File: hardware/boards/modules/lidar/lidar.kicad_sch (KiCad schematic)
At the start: 26 parts, among them J1 Conn_01x04_Socket, J2 Lidar, J3 Conn_01x03_Socket, J4 Conn_01x03_Socket, J5 Conn_01x03_Socket, J6 Conn_01x03_Socket, J7 Conn_01x05_Socket, Q1 AO3401A, SW1 SW_Push, U1 ATmega128A-A, Y1 8MHz

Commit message: REFACTO relinked every kicad projects
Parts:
- Q1: footprint Package_TO_SOT_SMD:SOT-23_Handsoldering -> Package_TO_SOT_SMD:SOT-23
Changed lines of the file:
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@@
+	)
+	(junction
+		(at 39.37 97.79)
+		(diameter 0)
+		(color 0 0 0 0)
 	)
 	(junction
@@
 	(wire
 		(pts
+			(xy 39.37 67.31) (xy 39.37 97.79)
+		)
+		(stroke
+			(width 0)
+			(type default)
+		)
+	)
+	(wire
+		(pts
 			(xy 162.56 152.4) (xy 162.56 140.97)
 		)
@@
 	(wire
 		(pts
+			(xy 30.48 67.31) (xy 39.37 67.31)
+		)
+		(stroke
+			(width 0)
+			(type default)
+		)
+	)
+	(wire
+		(pts
 			(xy 241.3 147.32) (xy 243.84 147.32)
 		)
@@
 	(wire
 		(pts
-			(xy 29.21 97.79) (xy 24.13 97.79)
+			(xy 24.13 97.79) (xy 30.48 97.79)
+		)
+		(stroke
+			(width 0)
+			(type default)
+		)
+	)
+	(wire
+		(pts
+			(xy 30.48 97.79) (xy 30.48 67.31)
 		)
 		(stroke
@@
 			)
 		)
-		(property "Footprint" "Package_TO_SOT_SMD:SOT-23_Handsoldering"
+		(property "Footprint" "Package_TO_SOT_SMD:SOT-23"
 			(at 238.76 81.915 0)
 			(effects

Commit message: updated main points of the lidar module schematic
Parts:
- removed J2: Lidar, Connector_PinHeader_2.54mm:PinHeader_1x04_P2.54mm_Vertical, symbol Connector:Conn_01x04_Socket
- removed J6: Conn_01x03_Socket, Connector_PinHeader_2.54mm:PinHeader_1x03_P2.54mm_Vertical, symbol Connector:Conn_01x03_Socket
- removed Q1: AO3401A, Package_TO_SOT_SMD:SOT-23, symbol Transistor_FET:AO3401A
- added C11, C12, C13: 100nF, Capacitor_SMD:C_0603_1608Metric_Pad1.08x0.95mm_HandSolder, symbol Device:C
- added C14: 4.7uF, Capacitor_SMD:C_0603_1608Metric_Pad1.08x0.95mm_HandSolder, symbol Device:C
- added J9: Lidar, Connector_PinHeader_2.54mm:PinHeader_1x04_P2.54mm_Vertical, symbol Connector:Conn_01x04_Socket
- added Q1: AO3400A, Package_TO_SOT_SMD:SOT-23, symbol Transistor_FET:AO3400A
- Y1: value 8MHz -> 16MHz
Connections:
- net 3V3: now also C11.1, C12.1, C13.1, C14.1
- net 5V: now also C5.1, C6.1, J9.1 (Pin_1); no longer R4.2
- net GND: now also C1.2, SW1.1, C11.2, C12.2, C13.2, C14.2, Q1.2 (S); no longer C5.2, C6.2, R5.2
- net LIDAR_PWM: now also J9.4 (Pin_4)
- net at R6.2: now also J9.2 (Pin_2)
- net SERVO_C_PWM: no longer names the net of U1.7 (PE5)
- new net: C5.2, C6.2, J9.3 (Pin_3), Q1.3 (D)
- new net: Q1.1 (G), R4.2, R5.2
- no-connect marks 33 -> 34
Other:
- note added: "- ISP (don't forget tx rx mixing) - still UART connector - no more adc nor debug connector (already have uart and isp)"
- moved on the sheet: C1

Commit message: lidar PCB
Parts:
- removed J3: Conn_01x03_Socket, Connector_PinHeader_2.54mm:PinHeader_1x03_P2.54mm_Vertical, symbol Connector:Conn_01x03_Socket
- removed J7: Conn_01x05_Socket, Connector_PinHeader_2.54mm:PinHeader_1x05_P2.54mm_Vertical, symbol Connector:Conn_01x05_Socket
- added J2: Dupont, Connector_PinHeader_2.54mm:PinHeader_1x06_P2.54mm_Vertical, symbol Connector:Conn_01x06_Socket
- C9: renamed from C5; footprint Capacitor_THT:CP_Radial_D5.0mm_P2.00mm -> Capacitor_SMD:CP_Elec_4x5.4
- D1: value LED -> GREEN
- D2: value LED -> RED
- J1: renamed from G1; value ~ -> JST; footprint Connector_PinHeader_2.54mm:PinHeader_1x05_P2.54mm_Vertical -> Connector_JST:JST_XH_B5B-XH-A_1x05_P2.50mm_Vertical
- J3: renamed from J1; value Conn_01x04_Socket -> Dupont
- J4: renamed from J9; value Lidar -> JST; footprint Connector_PinHeader_2.54mm:PinHeader_1x04_P2.54mm_Vertical -> Connector_JST:JST_XH_B4B-XH-A_1x04_P2.50mm_Vertical
- J5: renamed from J4; value Conn_01x03_Socket -> JST; footprint Connector_PinHeader_2.54mm:PinHeader_1x03_P2.54mm_Vertical -> Connector_JST:JST_XH_B3B-XH-A_1x03_P2.50mm_Vertical
- J6: renamed from J5; value Conn_01x03_Socket -> JST; footprint Connector_PinHeader_2.54mm:PinHeader_1x03_P2.54mm_Vertical -> Connector_JST:JST_XH_B3B-XH-A_1x03_P2.50mm_Vertical
- U1: value ATmega128A-A -> ATmega128A
- renumbered C6 to C10, C14 to C4, C12 to C5, C11 to C6, C13 to C7, C4 to C8, R5 to R4, R4 to R5
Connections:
- net 3V3: now also J2.5 (Pin_5)
- net GND: now also J2.6 (Pin_6)
- net LIDAR_EN: now also U1.6 (PE4); no longer U1.16 (PB6)
- net LIDAR_PWM: now also U1.5 (PE3); no longer U1.15 (PB5)
- net RST: now also J2.4 (Pin_4)
- net RX0: now also J3.2 (Pin_2), J2.3 (Pin_3); no longer J3.1 (Pin_1)
- net SERVO_A_PWM: now also U1.15 (PB5); no longer U1.5 (PE3)
- net SERVO_B_PWM: now also U1.16 (PB6); no longer U1.6 (PE4)
- net TX0: now also J3.1 (Pin_1), J2.2 (Pin_2); no longer J3.2 (Pin_2)
- net ADC0: no longer names the net of U1.61 (PF0)
- net ADC1: no longer names the net of U1.60 (PF1)
- net ADC2: no longer names the net of U1.59 (PF2)
- net DEBUG_0: no longer names the net of U1.10 (PB0)
- net DEBUG_1 renamed SCK
- net SCK: now also J2.1 (Pin_1)
- net DEBUG_2: no longer names the net of U1.12 (PB2)
- net DEBUG_3: no longer names the net of U1.13 (PB3)
- net DEBUG_4: no longer names the net of U1.14 (PB4)
- no-connect marks 34 -> 41
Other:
- note removed: "- ISP (don't forget tx rx mixing) - still UART connector - no more adc nor debug connector (already have uart and isp)"

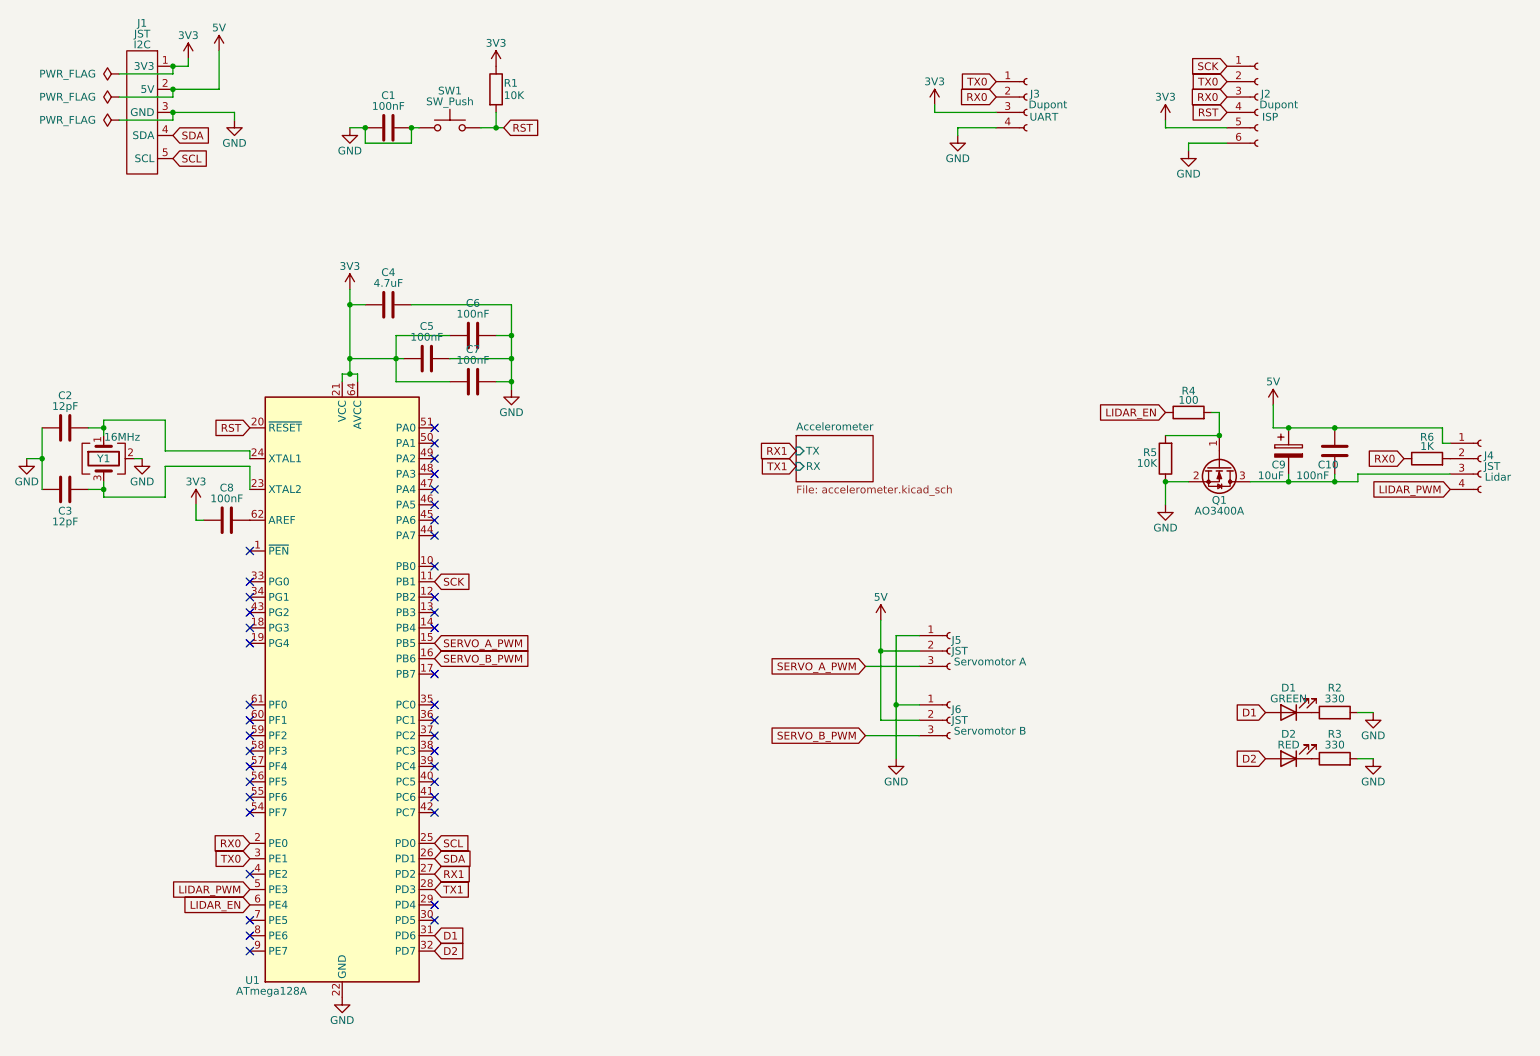
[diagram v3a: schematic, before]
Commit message: change kicad default to custom
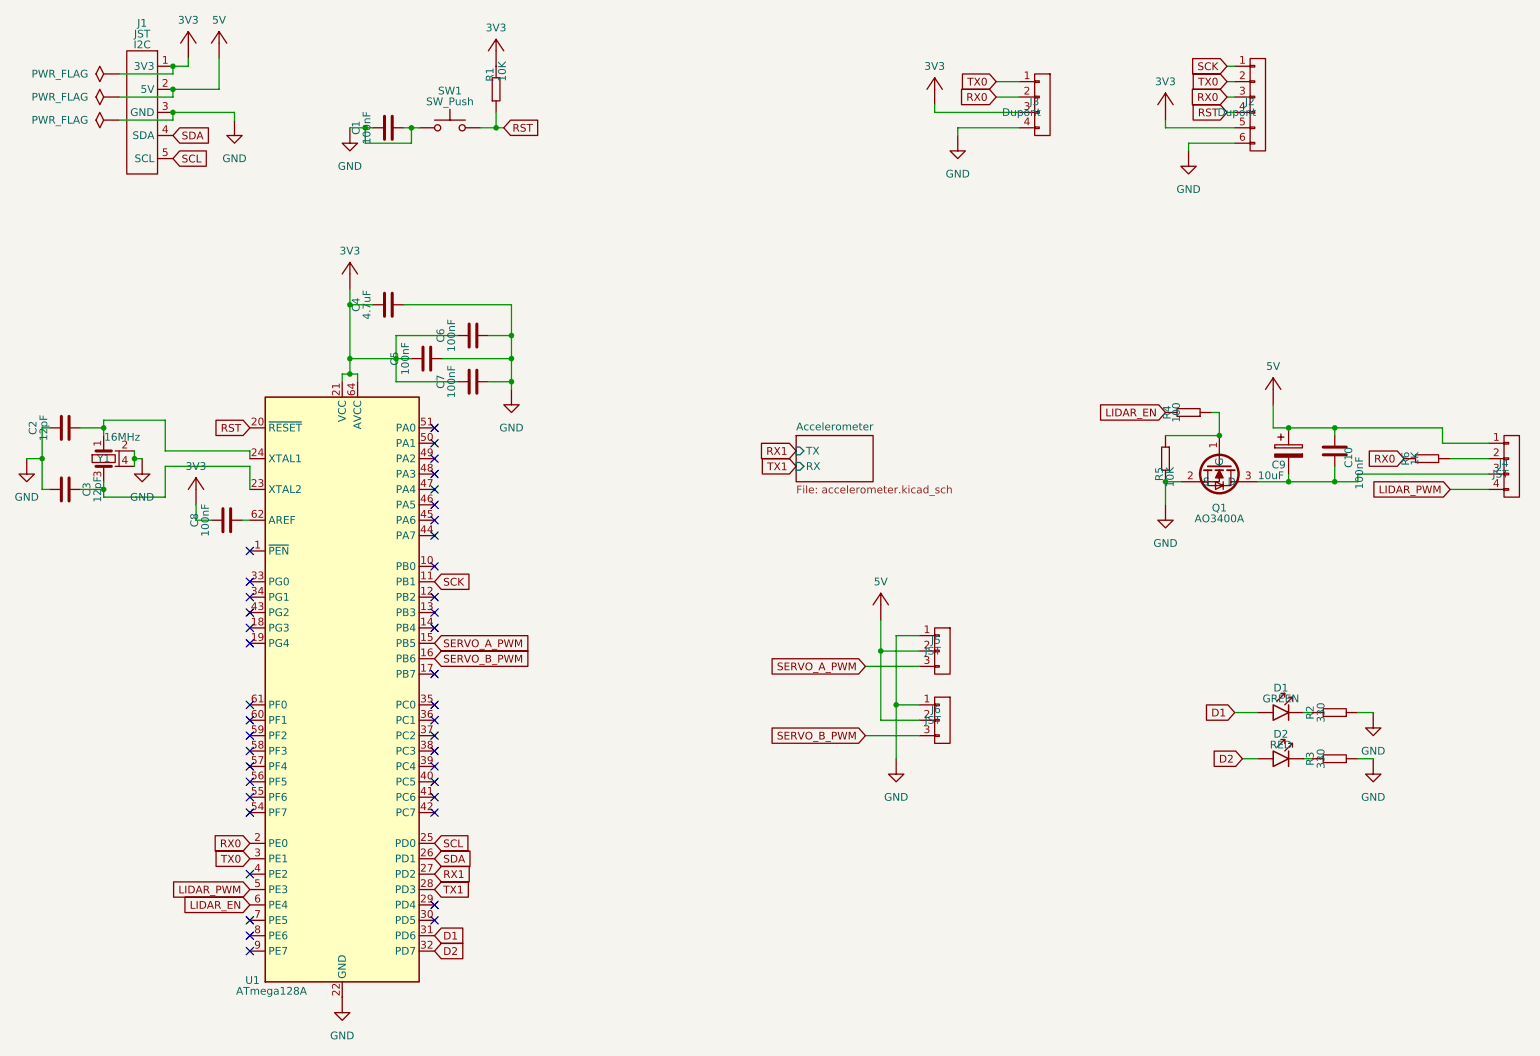
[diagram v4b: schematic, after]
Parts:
- C1, C10, C2, C3, C4, C5, C6, C7, C8: footprint Capacitor_SMD:C_0603_1608Metric_Pad1.08x0.95mm_HandSolder -> common:C_0603; symbol Device:C -> common:Capacitor
- C9: footprint Capacitor_SMD:CP_Elec_4x5.4 -> common:CP_Elec_4x5.4
- D1, D2: footprint LED_SMD:LED_0603_1608Metric_Pad1.05x0.95mm_HandSolder -> common:LED_0603; symbol Device:LED -> common:LED
- J1: footprint Connector_JST:JST_XH_B5B-XH-A_1x05_P2.50mm_Vertical -> connector:JST_1x5
- J2: footprint Connector_PinHeader_2.54mm:PinHeader_1x06_P2.54mm_Vertical -> connector:Pin_01x06; symbol Connector:Conn_01x06_Socket -> connector:Pin_01x06
- J3: footprint Connector_PinHeader_2.54mm:PinHeader_1x04_P2.54mm_Vertical -> connector:Pin_01x04; symbol Connector:Conn_01x04_Socket -> connector:Pin_01x04
- J4: symbol Connector:Conn_01x04_Socket -> connector:Pin_01x04
- J5, J6: symbol Connector:Conn_01x03_Socket -> connector:Pin_01x03
- Q1: footprint Package_TO_SOT_SMD:SOT-23 -> common:SOT-23; symbol Transistor_FET:AO3400A -> transistor:AO3400A
- R1, R2, R3, R4, R5, R6: footprint Resistor_SMD:R_0603_1608Metric_Pad0.98x0.95mm_HandSolder -> common:R_0603; symbol Device:R -> common:Resistor
- U1: symbol MCU_Microchip_ATmega:ATmega128A-A -> microchip:ATmega128A
- Y1: symbol Device:Crystal_GND24 -> common:Crystal_4Pins
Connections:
- net 3V3: now also C4.2, C5.2, C6.2, C7.2, C8.2, R1.2; no longer C4.1, C5.1, C6.1, C7.1, C8.1, R1.1
- net 5V: now also C10.2; no longer C10.1
- net GND: now also C4.1, C5.1, C6.1, C7.1, R2.1, R3.1, R5.2; no longer C4.2, C5.2, C6.2, C7.2, R2.2, R3.2, R5.1
- net LIDAR_EN: now also R4.2; no longer R4.1
- net RST: now also R1.1; no longer R1.2
- net RX0: now also R6.2; no longer R6.1
- net at J4.2: now also R6.1; no longer R6.2
- net at C9.2, J4.3, Q1.3 (D): now also C10.1; no longer C10.2
- net at D1.1 (K): now also R2.2; no longer R2.1
- net at U1.62 (AREF): now also C8.1; no longer C8.2
- net at D2.1 (K): now also R3.2; no longer R3.1
- new net: Q1.1 (G), R4.1, R5.1
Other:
- moved on the sheet: C1, C10, C2, C3, C4, C5, C6, C7, C8, R1, R2, R3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
